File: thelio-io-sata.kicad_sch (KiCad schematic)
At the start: 5 parts

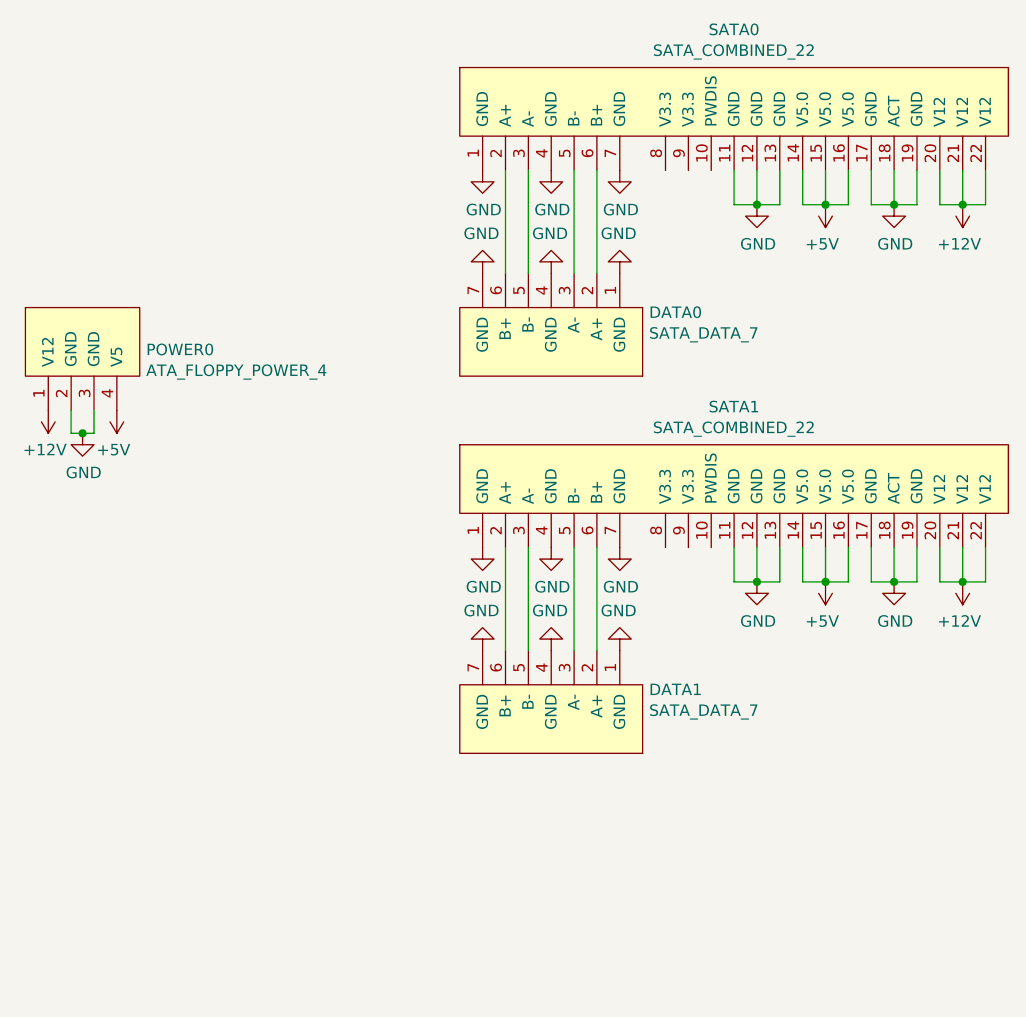
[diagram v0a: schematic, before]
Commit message: SATA 7 pin pinout the footprint was mirrored with pin 1 being where 7 should have been corrected footprint, mirrored symbol in schematic no physical changes, just pin numbers and net names give SATA data lines descriptive net names, +- suffix to all diff pair router
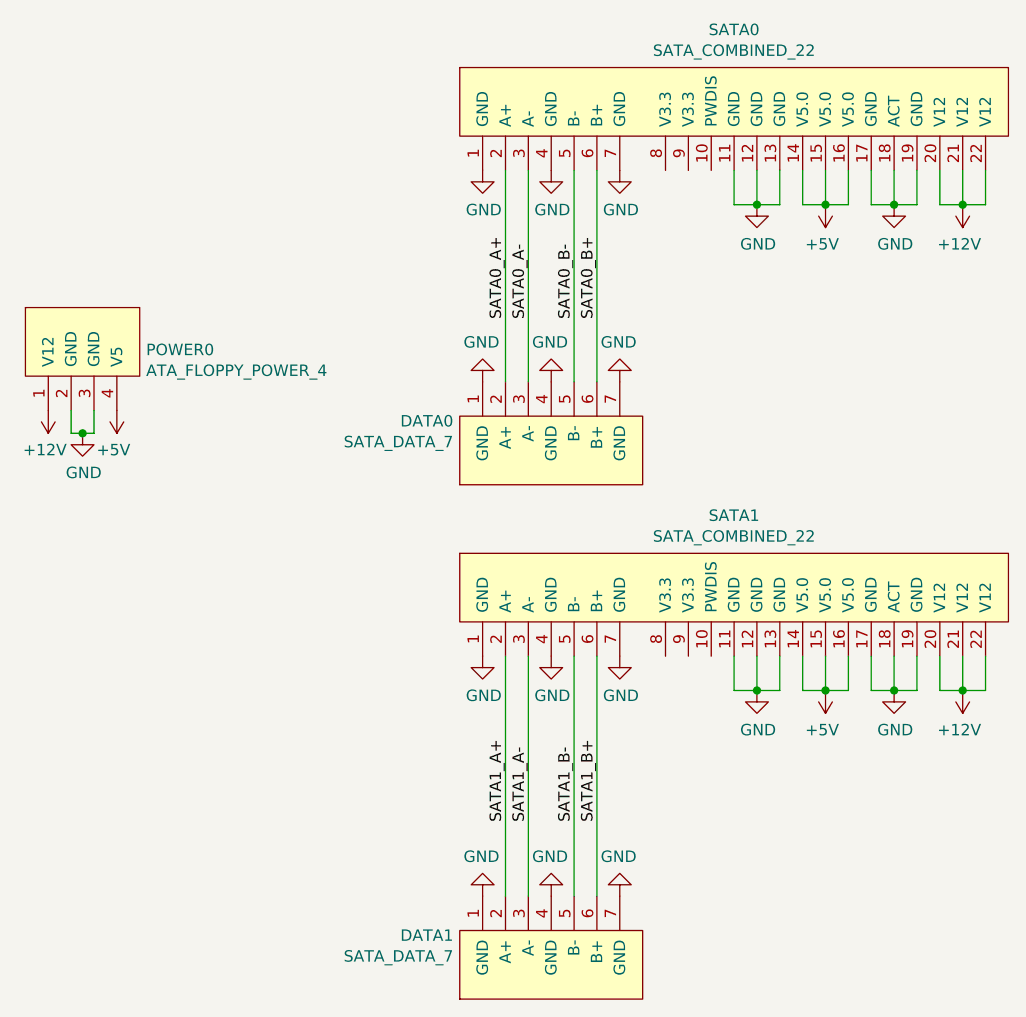
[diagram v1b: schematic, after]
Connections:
- net SATA0_A+: now reaches SATA0.2 (A+)
- net SATA0_A+: now also DATA0.2 (A+); no longer DATA0.6 (B+)
- net SATA0_A-: now reaches SATA0.3 (A-)
- net SATA0_A-: now also DATA0.3 (A-); no longer DATA0.5 (B-)
- net SATA0_B-: now reaches SATA0.5 (B-)
- net SATA0_B-: now also DATA0.5 (B-); no longer DATA0.3 (A-)
- net SATA0_B+: now reaches SATA0.6 (B+)
- net SATA0_B+: now also DATA0.6 (B+); no longer DATA0.2 (A+)
- net SATA1_A+: now reaches SATA1.2 (A+)
- net SATA1_A+: now also DATA1.2 (A+); no longer DATA1.6 (B+)
- net SATA1_A-: now reaches SATA1.3 (A-)
- net SATA1_A-: now also DATA1.3 (A-); no longer DATA1.5 (B-)
- net SATA1_B-: now reaches SATA1.5 (B-)
- net SATA1_B-: now also DATA1.5 (B-); no longer DATA1.3 (A-)
- net SATA1_B+: now reaches SATA1.6 (B+)
- net SATA1_B+: now also DATA1.6 (B+); no longer DATA1.2 (A+)
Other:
- moved on the sheet: DATA0, DATA1, SATA1

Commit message: part numbers, export settings
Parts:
- DATA0, DATA1: value SATA_DATA_7 -> 67800-5005; Manufacturer (none) -> Molex
- POWER0: value ATA_FLOPPY_POWER_4 -> 171825-4; Manufacturer (none) -> TE Connectivity
- SATA0, SATA1: value SATA_COMBINED_22 -> 1735284-4; Manufacturer (none) -> TE Connectivity
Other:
- title: (none) -> Thelio IO SATA
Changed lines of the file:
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@@
 (kicad_sch (version 20211123) (generator eeschema)
   (paper "A4")
+  (title_block
+    (title "Thelio IO SATA")
+    (date "2023-01-05")
+    (rev "1.0")
+  )
   (junction (at 114.3 108.585) (diameter 0) (color 0 0 0 0)
   )
@@
       (effects (font (size 1.27 1.27)) (justify right))
     )
-    (property "Value" "ATA_FLOPPY_POWER_4" (id 1) (at 38.8112 73.0504 90)
+    (property "Value" "171825-4" (id 1) (at 38.8112 73.0504 90)
       (effects (font (size 1.27 1.27)) (justify right))
     )
@@
     )
     (property "Datasheet" "lib/SATA/ATA_POWER_4.pdf" (id 3) (at 25.4 69.85 0)
+      (effects (font (size 1.27 1.27)) hide)
+    )
+    (property "Manufacturer" "TE Connectivity" (id 4) (at 31.75 69.85 0)
+      (effects (font (size 1.27 1.27)) hide)
+    )
+    (property "Description" "ATA floppy power connector" (id 5) (at 31.75 69.85 0)
       (effects (font (size 1.27 1.27)) hide)
     )
@@
     (in_bom yes) (on_board yes)
     (property "Reference" "SATA0" (id 0) (at 104.14 35.179 90))
-    (property "Value" "SATA_COMBINED_22" (id 1) (at 104.14 37.4904 90))
+    (property "Value" "1735284-4" (id 1) (at 104.14 37.4904 90))
     (property "Footprint" "SATA:SATA_COMBINED_22" (id 2) (at 93.98 39.37 0)
       (effects (font (size 1.27 1.27)) hide)
     )
     (property "Datasheet" "lib/SATA/SATA_COMBINED_22.pdf" (id 3) (at 93.98 39.37 0)
+      (effects (font (size 1.27 1.27)) hide)
+    )
+    (property "Manufacturer" "TE Connectivity" (id 4) (at 104.14 43.18 0)
+      (effects (font (size 1.27 1.27)) hide)
+    )
+    (property "Description" "SATA drive connector" (id 5) (at 104.14 43.18 0)
       (effects (font (size 1.27 1.27)) hide)
     )
@@
     (in_bom yes) (on_board yes)
     (property "Reference" "SATA1" (id 0) (at 104.14 89.154 90))
-    (property "Value" "SATA_COMBINED_22" (id 1) (at 104.14 91.4654 90))
+    (property "Value" "1735284-4" (id 1) (at 104.14 91.4654 90))
     (property "Footprint" "SATA:SATA_COMBINED_22" (id 2) (at 93.98 93.345 0)
       (effects (font (size 1.27 1.27)) hide)
     )
     (property "Datasheet" "lib/SATA/SATA_COMBINED_22.pdf" (id 3) (at 93.98 93.345 0)
+      (effects (font (size 1.27 1.27)) hide)
+    )
+    (property "Manufacturer" "TE Connectivity" (id 4) (at 104.14 97.155 0)
+      (effects (font (size 1.27 1.27)) hide)
+    )
+    (property "Description" "SATA drive connector" (id 5) (at 104.14 97.155 0)
       (effects (font (size 1.27 1.27)) hide)
     )
@@
       (effects (font (size 1.27 1.27)) (justify left))
     )
-    (property "Value" "SATA_DATA_7" (id 1) (at 72.9488 138.1252 90)
+    (property "Value" "67800-5005" (id 1) (at 72.9488 138.1252 90)
       (effects (font (size 1.27 1.27)) (justify left))
     )
@@
     )
     (property "Datasheet" "lib/SATA/SATA_DATA_7.pdf" (id 3) (at 72.39 146.685 0)
+      (effects (font (size 1.27 1.27)) hide)
+    )
+    (property "Manufacturer" "Molex" (id 4) (at 83.82 139.065 0)
+      (effects (font (size 1.27 1.27)) hide)
+    )
+    (property "Description" "SATA 7 pin cable connector" (id 5) (at 83.82 139.065 0)
       (effects (font (size 1.27 1.27)) hide)
     )
@@
       (effects (font (size 1.27 1.27)) (justify left))
     )
-    (property "Value" "SATA_DATA_7" (id 1) (at 72.9488 80.9752 90)
+    (property "Value" "67800-5005" (id 1) (at 72.9488 80.9752 90)
       (effects (font (size 1.27 1.27)) (justify left))
     )
@@
     )
     (property "Datasheet" "lib/SATA/SATA_DATA_7.pdf" (id 3) (at 72.39 89.535 0)
+      (effects (font (size 1.27 1.27)) hide)
+    )
+    (property "Manufacturer" "Molex" (id 4) (at 83.82 81.915 0)
+      (effects (font (size 1.27 1.27)) hide)
+    )
+    (property "Description" "SATA 7 pin cable connector" (id 5) (at 83.82 81.915 0)
       (effects (font (size 1.27 1.27)) hide)
     )
@@
     )
     (path "/83769fbe-00d5-44bf-984c-6bcd6444feac"
-      (reference "DATA0") (unit 1) (value "SATA_DATA_7") (footprint "SATA:SATA_DATA_7")
+      (reference "DATA0") (unit 1) (value "67800-5005") (footprint "SATA:SATA_DATA_7")
     )
     (path "/77cf97a8-733f-4844-b739-32296b0bf70e"
-      (reference "DATA1") (unit 1) (value "SATA_DATA_7") (footprint "SATA:SATA_DATA_7")
+      (reference "DATA1") (unit 1) (value "67800-5005") (footprint "SATA:SATA_DATA_7")
     )
     (path "/00000000-0000-0000-0000-00005b9b7b19"
-      (reference "POWER0") (unit 1) (value "ATA_FLOPPY_POWER_4") (footprint "SATA:ATA_FLOPPY_POWER_4")
+      (reference "POWER0") (unit 1) (value "171825-4") (footprint "SATA:ATA_FLOPPY_POWER_4")
     )
     (path "/38395bfc-58fa-4d48-a8ef-b7c78e8545e9"
-      (reference "SATA0") (unit 1) (value "SATA_COMBINED_22") (footprint "SATA:SATA_COMBINED_22")
+      (reference "SATA0") (unit 1) (value "1735284-4") (footprint "SATA:SATA_COMBINED_22")
     )
     (path "/54c19e9d-a3f7-4b53-b8ac-ff4830ed3a4c"
-      (reference "SATA1") (unit 1) (value "SATA_COMBINED_22") (footprint "SATA:SATA_COMBINED_22")
-    )
-  )
+      (reference "SATA1") (unit 1) (value "1735284-4") (footprint "SATA:SATA_COMBINED_22")
+    )
+  )
